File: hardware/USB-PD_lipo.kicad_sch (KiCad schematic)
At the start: 13 parts, among them J1 TC2030-SWD, U2 STM32G0C1KETxN

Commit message: Added BMS and DC/DC
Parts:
- removed BT1, BT2: Battery_Cell, Battery:BatteryHolder_Keystone_1042_1x18650, symbol Device:Battery_Cell
- removed C7, C8, C9: 100nF, Capacitor_SMD:C_0402_1005Metric, symbol Device:C_Small
- removed J1: TC2030-SWD, Connector:Tag-Connect_TC2030-IDC-FP_2x03_P1.27mm_Vertical, symbol Connector:Conn_ARM_SWD_TagConnect_TC2030
- removed R4, R5: R_Small, Resistor_SMD:R_0603_1608Metric, symbol Device:R_Small
- removed R8, R9: 10k, Resistor_SMD:R_0603_1608Metric, symbol Device:R_Small
- removed U2: STM32G0C1KETxN, Package_QFP:LQFP-32_7x7mm_P0.8mm, symbol MCU_ST_STM32G0:STM32G0C1KETxN
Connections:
- net SCL renamed BMS/SCL
- net SDA renamed BMS/SDA
- no-connect marks 1 -> 3
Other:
- removed sheet 12V-5A-boost
- added sheet BMS (BMS.kicad_sch)
- added sheet DC-DC (DC-DC.kicad_sch)
- added sheet MCU (MCU.kicad_sch)
- sheet USB-PD dual role protection ports: added USB_GND_SHUNT+, USB_GND_SHUNT-; removed none
- note added: "I2C: 0x34"
- note added: "I2C: 0x67"
- note added: "I2C: 0x6B"
- note added: "TODO: - DC/DC: - Symbol MR - Footprint - Footprint MR - Sizing / calculation - USB: - ECMF02-2AMX6: - Symbol - Footprint (?) - DFN 5x6 dual mosfet footprint"
- note removed: "BQ25887"

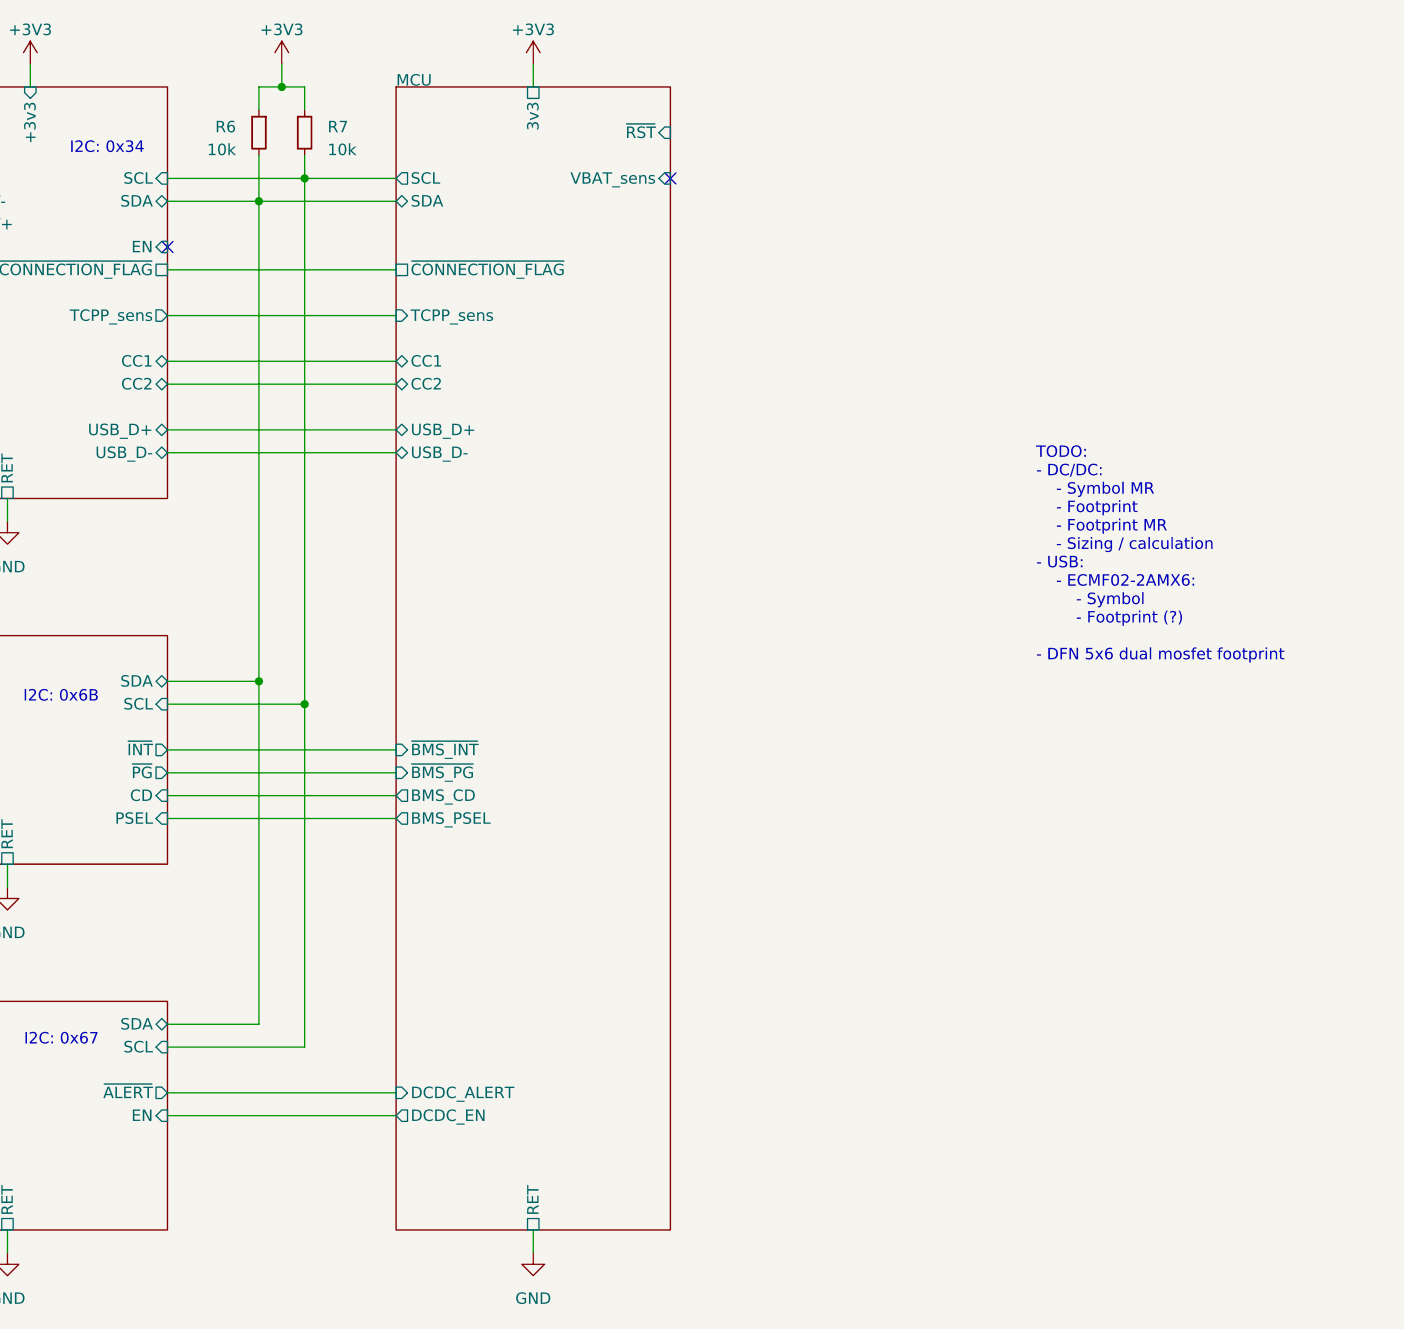
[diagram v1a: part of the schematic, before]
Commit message: Some routing and pinout changes
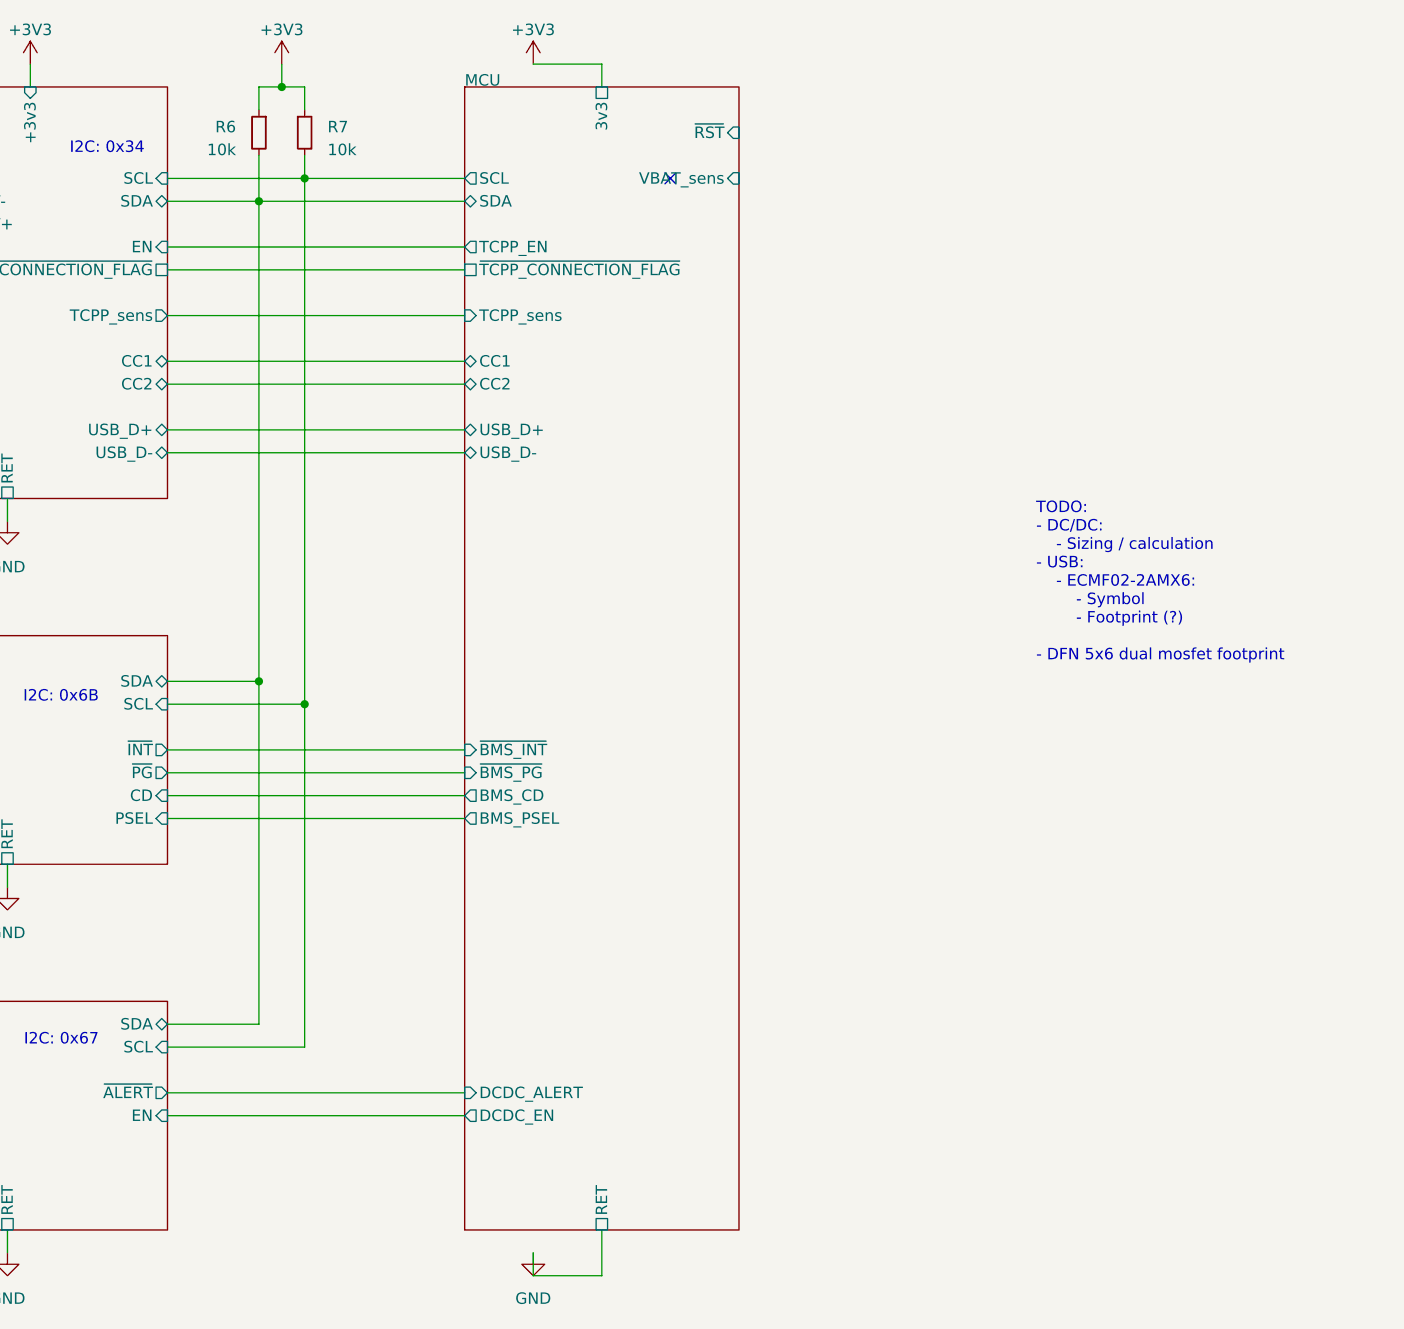
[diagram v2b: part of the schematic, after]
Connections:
- no-connect marks 3 -> 2
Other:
- sheet MCU ports: added TCPP_EN, ~{TCPP_CONNECTION_FLAG}; removed ~{CONNECTION_FLAG}
- note added: "TODO: - DC/DC: - Sizing / calculation - USB: - ECMF02-2AMX6: - Symbol - Footprint (?) - DFN 5x6 dual mosfet footprint"
- note removed: "TODO: - DC/DC: - Symbol MR - Footprint - Footprint MR - Sizing / calculation - USB: - ECMF02-2AMX6: - Symbol - Footprint (?) - DFN 5x6 dual mosfet footprint"
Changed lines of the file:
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@@
   (no_connect (at 162.56 45.72))
   (no_connect (at 71.12 43.18))
-  (no_connect (at 106.68 53.34))
-  (wire (pts (xy 106.68 114.3) (xy 132.08 114.3))
-    (stroke (width 0) (type default))
-  )
-  (wire (pts (xy 106.68 68.58) (xy 132.08 68.58))
+  (wire (pts (xy 106.68 114.3) (xy 139.7 114.3))
+    (stroke (width 0) (type default))
+  )
+  (wire (pts (xy 106.68 68.58) (xy 139.7 68.58))
     (stroke (width 0) (type default))
   )
@@
     (stroke (width 0) (type default))
   )
-  (wire (pts (xy 147.32 162.56) (xy 147.32 165.1))
+  (wire (pts (xy 154.94 162.56) (xy 154.94 167.64))
     (stroke (width 0) (type default))
   )
@@
     (stroke (width 0) (type default))
   )
-  (wire (pts (xy 106.68 66.04) (xy 132.08 66.04))
+  (wire (pts (xy 106.68 66.04) (xy 139.7 66.04))
     (stroke (width 0) (type default))
   )
@@
     (stroke (width 0) (type default))
   )
-  (wire (pts (xy 106.68 76.2) (xy 132.08 76.2))
+  (wire (pts (xy 106.68 76.2) (xy 139.7 76.2))
     (stroke (width 0) (type default))
   )
@@
     (stroke (width 0) (type default))
   )
-  (wire (pts (xy 106.68 111.76) (xy 132.08 111.76))
-    (stroke (width 0) (type default))
-  )
-  (wire (pts (xy 147.32 33.02) (xy 147.32 35.56))
+  (wire (pts (xy 106.68 111.76) (xy 139.7 111.76))
+    (stroke (width 0) (type default))
+  )
+  (wire (pts (xy 154.94 33.02) (xy 154.94 35.56))
     (stroke (width 0) (type default))
   )
@@
     (stroke (width 0) (type default))
   )
-  (wire (pts (xy 106.68 55.88) (xy 132.08 55.88))
+  (wire (pts (xy 106.68 55.88) (xy 139.7 55.88))
     (stroke (width 0) (type default))
   )
@@
     (stroke (width 0) (type default))
   )
-  (wire (pts (xy 116.84 48.26) (xy 132.08 48.26))
+  (wire (pts (xy 116.84 48.26) (xy 139.7 48.26))
+    (stroke (width 0) (type default))
+  )
+  (wire (pts (xy 147.32 167.64) (xy 147.32 165.1))
     (stroke (width 0) (type default))
   )
@@
     (stroke (width 0) (type default))
   )
-  (wire (pts (xy 106.68 147.32) (xy 132.08 147.32))
+  (wire (pts (xy 106.68 147.32) (xy 139.7 147.32))
     (stroke (width 0) (type default))
   )
@@
     (stroke (width 0) (type default))
   )
-  (wire (pts (xy 121.92 45.72) (xy 132.08 45.72))
+  (wire (pts (xy 121.92 45.72) (xy 139.7 45.72))
     (stroke (width 0) (type default))
   )
@@
     (stroke (width 0) (type default))
   )
-  (wire (pts (xy 106.68 149.86) (xy 132.08 149.86))
+  (wire (pts (xy 106.68 149.86) (xy 139.7 149.86))
     (stroke (width 0) (type default))
   )
@@
     (stroke (width 0) (type default))
   )
-  (wire (pts (xy 106.68 73.66) (xy 132.08 73.66))
+  (wire (pts (xy 106.68 73.66) (xy 139.7 73.66))
     (stroke (width 0) (type default))
   )
@@
     (stroke (width 0) (type default))
   )
-  (wire (pts (xy 106.68 60.96) (xy 132.08 60.96))
+  (wire (pts (xy 106.68 60.96) (xy 139.7 60.96))
+    (stroke (width 0) (type default))
+  )
+  (wire (pts (xy 106.68 53.34) (xy 139.7 53.34))
     (stroke (width 0) (type default))
   )
@@
     (stroke (width 0) (type default))
   )
-  (wire (pts (xy 106.68 109.22) (xy 132.08 109.22))
+  (wire (pts (xy 154.94 33.02) (xy 147.32 33.02))
+    (stroke (width 0) (type default))
+  )
+  (wire (pts (xy 106.68 109.22) (xy 139.7 109.22))
     (stroke (width 0) (type default))
   )
@@
     (stroke (width 0) (type default))
   )
-  (wire (pts (xy 106.68 116.84) (xy 132.08 116.84))
+  (wire (pts (xy 106.68 116.84) (xy 139.7 116.84))
     (stroke (width 0) (type default))
   )
@@
   )
   (wire (pts (xy 60.96 68.58) (xy 60.96 71.12))
+    (stroke (width 0) (type default))
+  )
+  (wire (pts (xy 154.94 167.64) (xy 147.32 167.64))
     (stroke (width 0) (type default))
   )
@@
     (effects (font (size 1.27 1.27)) (justify right bottom))
   )
-  (text "TODO:\n- DC/DC:\n	- Symbol MR\n	- Footprint\n	- Footprint MR\n	- Sizing / calculation\n- USB:\n	- ECMF02-2AMX6:\n		- Symbol\n		- Footprint (?)\n\n- DFN 5x6 dual mosfet footprint\n\n"
+  (text "TODO:\n- DC/DC:\n	- Sizing / calculation\n- USB:\n	- ECMF02-2AMX6:\n		- Symbol\n		- Footprint (?)\n\n- DFN 5x6 dual mosfet footprint\n\n"
     (at 203.2 101.6 0)
     (effects (font (size 1.27 1.27)) (justify left bottom))
@@
   (text "I2C: 0x67" (at 99.06 142.24 0)
     (effects (font (size 1.27 1.27)) (justify right bottom))
+  )
+  (netclass_flag "" (length 2.54) (shape round) (at 124.46 76.2 180) (fields_autoplaced)
+    (effects (font (size 1.27 1.27)) (justify right bottom))
+    (property "Netclass" "USB_data" (at 125.1585 78.74 0)
+      (effects (font (size 1.27 1.27) italic) (justify left))
+    )
+  )
+  (netclass_flag "" (length 2.54) (shape round) (at 124.46 73.66 0) (fields_autoplaced)
+    (effects (font (size 1.27 1.27)) (justify left bottom))
+    (property "Netclass" "USB_data" (at 125.1585 71.12 0)
+      (effects (font (size 1.27 1.27) italic) (justify left))
+    )
   )
   (symbol (lib_id "power:+3V3") (at 119.38 33.02 0) (unit 1)
@@
     )
   )
-  (sheet (at 132.08 35.56) (size 30.48 127)
+  (sheet (at 139.7 35.56) (size 30.48 127)
     (stroke (width 0.1524) (type solid))
     (fill (color 0 0 0 0.0000))
-    (property "Sheetname" "MCU" (at 132.08 35.56 0)
+    (property "Sheetname" "MCU" (at 139.7 35.56 0)
       (effects (font (size 1.27 1.27)) (justify left bottom))
     )
-    (property "Sheetfile" "MCU.kicad_sch" (at 132.08 81.8646 0)
+    (property "Sheetfile" "MCU.kicad_sch" (at 139.7 81.8646 0)
       (effects (font (size 1.27 1.27)) (justify left top) hide)
     )
-    (pin "SCL" output (at 132.08 45.72 180)
-      (effects (font (size 1.27 1.27)) (justify left))
-    )
-    (pin "RET" passive (at 147.32 162.56 270)
-      (effects (font (size 1.27 1.27)) (justify left))
-    )
-    (pin "TCPP_sens" input (at 132.08 60.96 180)
-      (effects (font (size 1.27 1.27)) (justify left))
-    )
-    (pin "VBAT_sens" input (at 162.56 45.72 0)
-      (effects (font (size 1.27 1.27)) (justify right))
-    )
-    (pin "USB_D+" bidirectional (at 132.08 73.66 180)
-      (effects (font (size 1.27 1.27)) (justify left))
-    )
-    (pin "USB_D-" bidirectional (at 132.08 76.2 180)
-      (effects (font (size 1.27 1.27)) (justify left))
-    )
-    (pin "~{RST}" input (at 162.56 40.64 0)
-      (effects (font (size 1.27 1.27)) (justify right))
-    )
-    (pin "CC1" bidirectional (at 132.08 66.04 180)
-      (effects (font (size 1.27 1.27)) (justify left))
-    )
-    (pin "SDA" bidirectional (at 132.08 48.26 180)
-      (effects (font (size 1.27 1.27)) (justify left))
-    )
-    (pin "CC2" bidirectional (at 132.08 68.58 180)
-      (effects (font (size 1.27 1.27)) (justify left))
-    )
-    (pin "~{CONNECTION_FLAG}" passive (at 132.08 55.88 180)
-      (effects (font (size 1.27 1.27)) (justify left))
-    )
-    (pin "3v3" passive (at 147.32 35.56 90)
-      (effects (font (size 1.27 1.27)) (justify right))
-    )
-    (pin "BMS_CD" output (at 132.08 114.3 180)
-      (effects (font (size 1.27 1.27)) (justify left))
-    )
-    (pin "~{BMS_INT}" input (at 132.08 109.22 180)
-      (effects (font (size 1.27 1.27)) (justify left))
-    )
-    (pin "~{BMS_PG}" input (at 132.08 111.76 180)
-      (effects (font (size 1.27 1.27)) (justify left))
-    )
-    (pin "BMS_PSEL" output (at 132.08 116.84 180)
-      (effects (font (size 1.27 1.27)) (justify left))
-    )
-    (pin "DCDC_EN" output (at 132.08 149.86 180)
-      (effects (font (size 1.27 1.27)) (justify left))
-    )
-    (pin "DCDC_ALERT" input (at 132.08 147.32 180)
-      (effects (font (size 1.27 1.27)) (justify left))
-    )
+    (pin "SCL" output (at 139.7 45.72 180)
+      (effects (font (size 1.27 1.27)) (justify left))
+    )
+    (pin "RET" passive (at 154.94 162.56 270)
+      (effects (font (size 1.27 1.27)) (justify left))
+    )
+    (pin "TCPP_sens" input (at 139.7 60.96 180)
+      (effects (font (size 1.27 1.27)) (justify left))
+    )
+    (pin "VBAT_sens" input (at 170.18 45.72 0)
+      (effects (font (size 1.27 1.27)) (justify right))
+    )
+    (pin "USB_D+" bidirectional (at 139.7 73.66 180)
+      (effects (font (size 1.27 1.27)) (justify left))
+    )
+    (pin "USB_D-" bidirectional (at 139.7 76.2 180)
+      (effects (font (size 1.27 1.27)) (justify left))
+    )
+    (pin "~{RST}" input (at 170.18 40.64 0)
+      (effects (font (size 1.27 1.27)) (justify right))
+    )
+    (pin "CC1" bidirectional (at 139.7 66.04 180)
+      (effects (font (size 1.27 1.27)) (justify left))
+    )
+    (pin "SDA" bidirectional (at 139.7 48.26 180)
+      (effects (font (size 1.27 1.27)) (justify left))
+    )
+    (pin "CC2" bidirectional (at 139.7 68.58 180)
+      (effects (font (size 1.27 1.27)) (justify left))
+    )
+    (pin "3v3" passive (at 154.94 35.56 90)
+      (effects (font (size 1.27 1.27)) (justify right))
+    )
+    (pin "BMS_CD" output (at 139.7 114.3 180)
+      (effects (font (size 1.27 1.27)) (justify left))
+    )
+    (pin "~{BMS_INT}" input (at 139.7 109.22 180)
+      (effects (font (size 1.27 1.27)) (justify left))
+    )
+    (pin "~{BMS_PG}" input (at 139.7 111.76 180)
+      (effects (font (size 1.27 1.27)) (justify left))
+    )
+    (pin "BMS_PSEL" output (at 139.7 116.84 180)
+      (effects (font (size 1.27 1.27)) (justify left))
+    )
+    (pin "DCDC_EN" output (at 139.7 149.86 180)
+      (effects (font (size 1.27 1.27)) (justify left))
+    )
+    (pin "DCDC_ALERT" input (at 139.7 147.32 180)
+      (effects (font (size 1.27 1.27)) (justify left))
+    )
+    (pin "TCPP_EN" output (at 139.7 53.34 180)
+      (effects (font (size 1.27 1.27)) (justify left))
+    )
+    (pin "~{TCPP_CONNECTION_FLAG}" passive (at 139.7 55.88 180)
+      (effects (font (size 1.27 1.27)) (justify left))
+    )
